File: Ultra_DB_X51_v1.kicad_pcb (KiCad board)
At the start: 2 copper layers, 178 x 145 mm, 144 parts, among them IC1 L293D, J1 USB_2, K1 RELAYPTH, K2 RELAYPTH, K3 I2C, K4 CONN_3, P1 CONN_5, P10 CONN_8, P11 CONN_4, P12 CONN_8, P13 CONN_1, P14 CONN_1, P15 CONN_1, P16 CONN_8, P17 CONN_8, P18 CONN_7, P19 CONN_1, P2 CONN_5, P3 CONN_5, P4 CONN_1, P5 CONN_5X2, P6 CONN_1, P7 CONN_8, P8 CONN_8, P9 CONN_8, Q1 BC557, Q2 BC548, Q3 BC548, Q4 BC548, Q5 BC548, Q6 BC548, Q7 BC548, Q8 BC548, SW1 SPST, SW10 5, SW11 6, SW12 7, SW13 8, SW14 1, SW15 2, SW16 3, SW17 4, SW18 SPST, SW19 INT0, SW2 C, SW20 INT1, SW3 D, SW4 E, SW5 F, SW6 9, SW7 0, SW8 A, SW9 B, U1 7805, U10 CP2102, U2 24C16, U3 DS1307, U4 BATTERY, U5 LM555N_XL, U6 ADC0808, U7 AT89S52, X1 CRYSTAL, X3 11.0592MHz

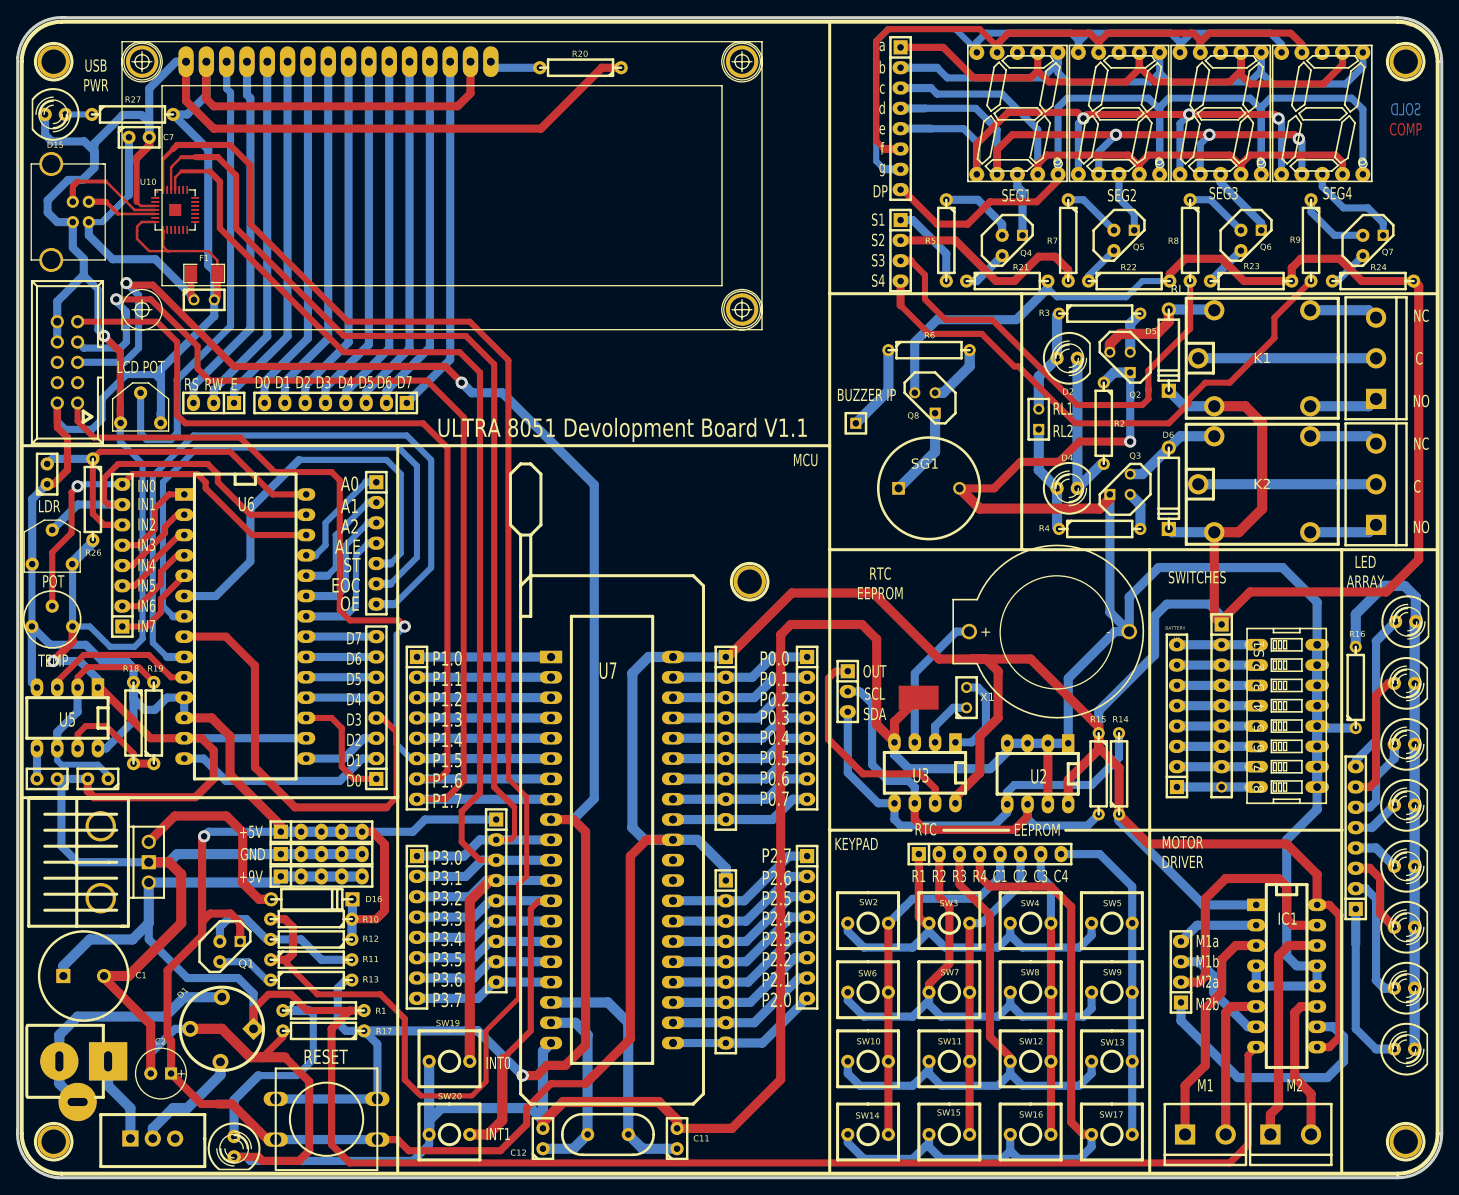
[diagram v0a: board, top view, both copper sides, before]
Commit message: Ver1.2
1. Mounting holes for slide switch
2. Nomenclature for all the ident.
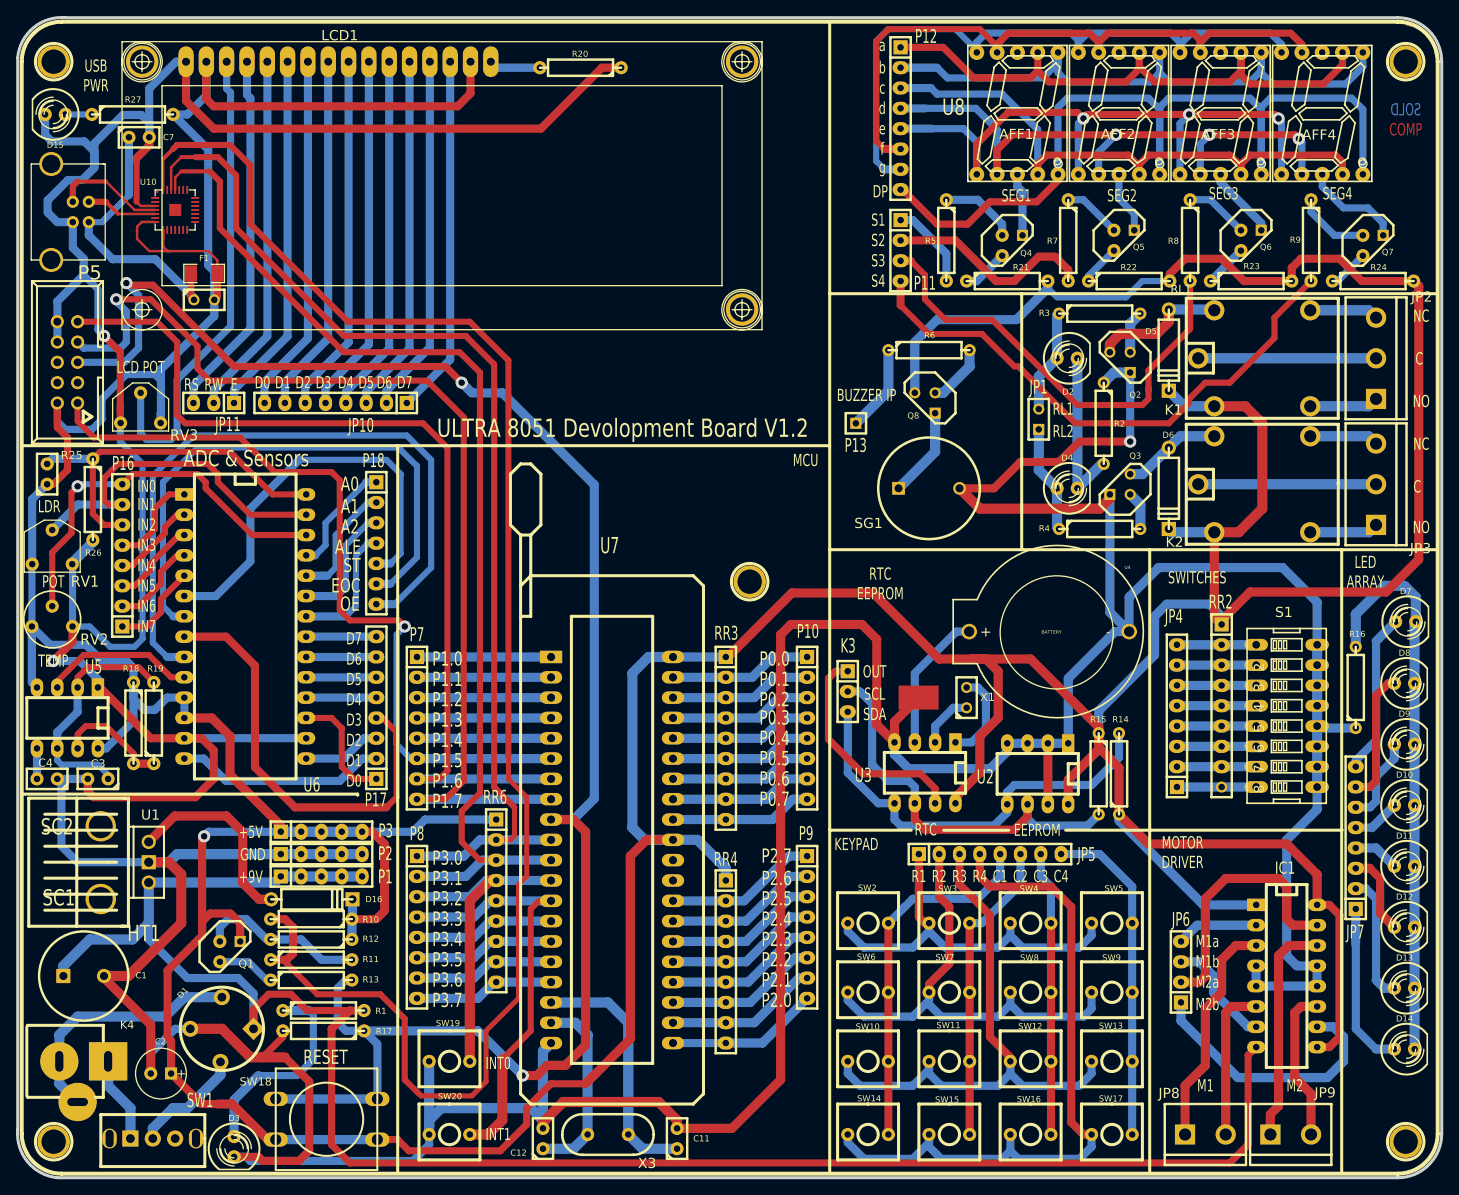
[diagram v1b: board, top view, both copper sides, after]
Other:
- board text added: "ADC & Sensors"
- board text added: "HT1"
- board text added: "SC1"
- board text added: "SC2"
- board text added: "U8"
- board text added: "ULTRA 8051 Devolopment Board V1.2"
- board text removed: "ULTRA 8051 Devolopment Board V1.1"
